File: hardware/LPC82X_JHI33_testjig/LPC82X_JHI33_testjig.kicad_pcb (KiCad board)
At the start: 2 copper layers, 23.6 x 23.5 mm, 80 parts, among them J1 LPC82XJHI33_LEFT, J2 LPC82XJHI33_RIGHT, J3 JTAG_2X05

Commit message: routing completed
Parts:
- removed C7: 2.2u, SquantorRcl:C_0805
- added H1: MountingHole, MountingHole:MountingHole_3.2mm_M3_Pad_Via, F.Cu at (73.7, 99.1)
- added H2: MountingHole, MountingHole:MountingHole_3.2mm_M3_Pad_Via, F.Cu at (73.7, 114.3)
- added H3: MountingHole, MountingHole:MountingHole_3.2mm_M3_Pad_Via, F.Cu at (104.1, 114.3)
- added H4: MountingHole, MountingHole:MountingHole_3.2mm_M3_Pad_Via, F.Cu at (104.1, 99.1)
- C1, C10, C11, C12, C13, C14, C15, C16, C17, C18, C19, C2, C20, C21, C22, C23, C24, C25, C3, C4, C5, C6, C8, C9: value 2.2u -> 1u; footprint SquantorRcl:C_0805 -> SquantorRcl:C_0402; moved to B.Cu
- J1: footprint SquantorConnectorsNamed:LPC82XJHI33_breakout_left -> SquantorConnectors:Header-0254-2X09-H015
- J2: footprint SquantorConnectorsNamed:LPC82XJHI33_breakout_right -> SquantorConnectors:Header-0254-2X09-H015
- R1, R11, R13, R15, R17, R19, R2, R21, R23, R25, R27, R29, R31, R33, R35, R37, R39, R41, R43, R45, R47, R49, R5, R51, R7, R9: footprint SquantorRcl:R_0603_hand -> SquantorRcl:R_0402_hand
- R10, R12, R14, R16, R18, R20, R22, R24, R26, R28, R30, R32, R34, R36, R38, R4, R40, R42, R44, R46, R48, R50, R6, R8: footprint SquantorRcl:R_0603_hand -> SquantorRcl:R_0402_hand; moved to B.Cu
- moved R12 82.3 mm to (94.0, 108.3)
- moved C5 80.8 mm to (91.7, 108.3), turned to 180 degrees
- moved R6 80.8 mm to (94.0, 101.8)
- moved C2 78.7 mm to (91.7, 101.8), turned to 180 degrees
- moved R22 70.9 mm to (94.0, 112.2)
- moved C11 69.7 mm to (91.7, 112.2), turned to 180 degrees
- moved R16 68.8 mm to (94.0, 110.9)
- moved R8 68.1 mm to (94.0, 105.7)
- moved R32 67.2 mm to (83.8, 104.4), turned to 180 degrees
- moved C8 67.2 mm to (91.7, 110.9), turned to 180 degrees
- moved R33 66.7 mm to (83.8, 104.4), turned to 180 degrees
- moved C3 66.0 mm to (91.7, 105.7), turned to 180 degrees
- moved R26 65.6 mm to (83.8, 100.5), turned to 180 degrees
- moved R27 65.6 mm to (83.8, 100.5), turned to 180 degrees
- moved C16 60.7 mm to (86.1, 104.4)
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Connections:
- J1 pad 10: /PIO0_26 -> /PIO0_27
- J1 pad 11: /PIO0_25 -> /PIO0_24
- J1 pad 12: /PIO0_24 -> /PIO0_25
- J1 pad 13: /PIO0_15 -> /PIO0_1
- J1 pad 14: /PIO0_1 -> /PIO0_15
- J1 pad 3: /PIO0_28 -> /PIO0_3
- J1 pad 4: /PIO0_3 -> /PIO0_28
- J1 pad 5: /PIO0_2 -> /PIO0_11
- J1 pad 6: /PIO0_11 -> /PIO0_2
- J1 pad 7: /PIO0_10 -> /PIO0_16
- J1 pad 8: /PIO0_16 -> /PIO0_10
- J1 pad 9: /PIO0_27 -> /PIO0_26
- J2 pad 10: /PIO0_21 -> /PIO0_20
- J2 pad 11: /PIO0_22 -> /PIO0_23
- J2 pad 12: /PIO0_23 -> /PIO0_22
- J2 pad 13: /PIO0_14 -> /PIO0_0
- J2 pad 14: /PIO0_0 -> /PIO0_14
- J2 pad 15: /PIO0_6 -> /PIO0_7
- J2 pad 16: /PIO0_7 -> /PIO0_6
- J2 pad 3: /PIO0_4 -> /PIO0_12
- J2 pad 4: /PIO0_12 -> /PIO0_4
- J2 pad 5: /PIO0_13 -> /PIO0_17
- J2 pad 6: /PIO0_17 -> /PIO0_13
- J2 pad 7: /PIO0_18 -> /PIO0_19
- J2 pad 8: /PIO0_19 -> /PIO0_18
- J2 pad 9: /PIO0_20 -> /PIO0_21
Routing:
- net /Digital_stimulus: track 0.00 -> 41.8 mm
- net /VDD: track 0.00 -> 41.6 mm
- net /VSS: track 12.7 -> 0.00 mm
- net /PIO0_15: track 0.00 -> 10.6 mm
- net /PIO0_7: track 0.00 -> 10.6 mm
- net /PIO0_25: track 0.00 -> 10.5 mm
- net /PIO0_0: track 0.00 -> 10.4 mm
- net /PIO0_17: track 0.00 -> 10.3 mm
- net /PIO0_10: track 0.00 -> 10.3 mm
- net /PIO0_27: track 0.00 -> 10.3 mm
- net /PIO0_23: track 0.00 -> 10.3 mm
- net /PIO0_19: track 0.00 -> 10.3 mm
- net /PIO0_28: track 0.00 -> 10.3 mm
- net /PIO0_21: track 0.00 -> 10.2 mm
- net /PIO0_12: track 0.00 -> 10.1 mm
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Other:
- board size 23.6 x 23.5 mm -> 38.8 x 23.5 mm

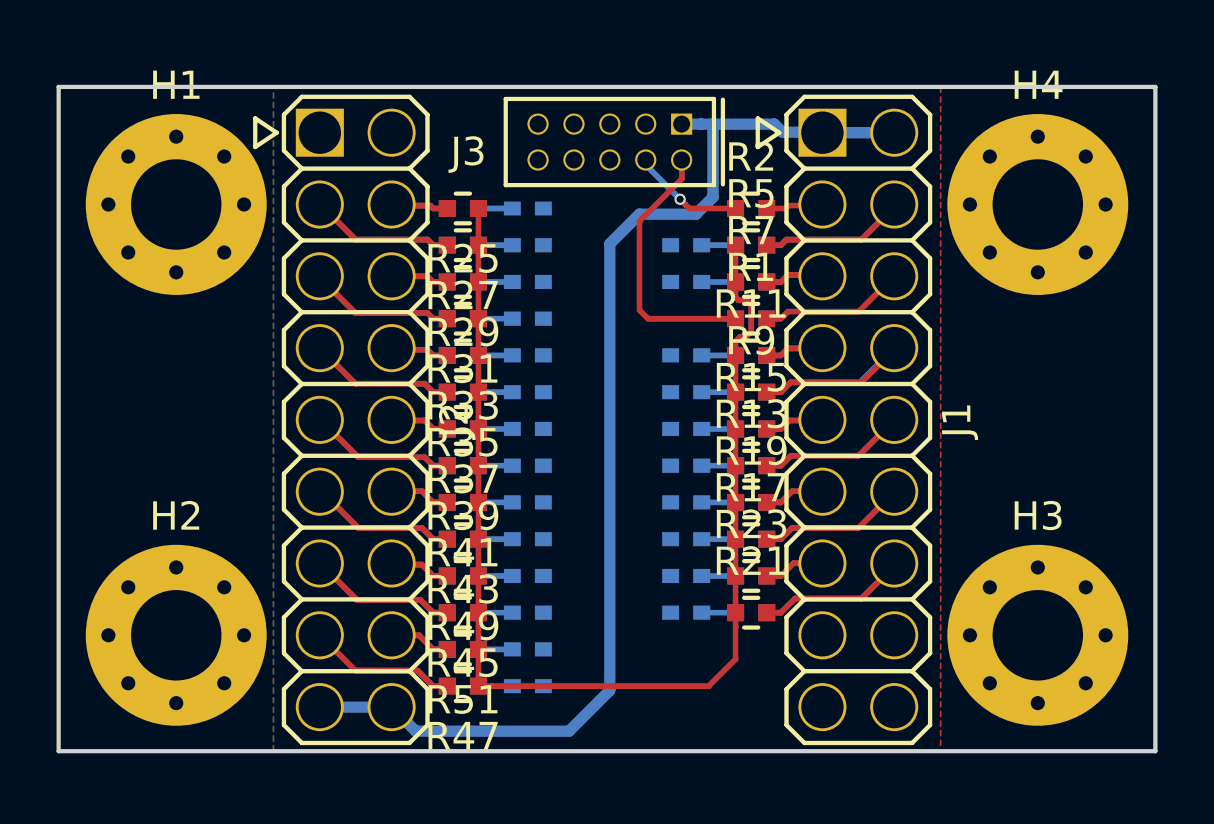
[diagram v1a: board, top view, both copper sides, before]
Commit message: silk placement completed (where possible)
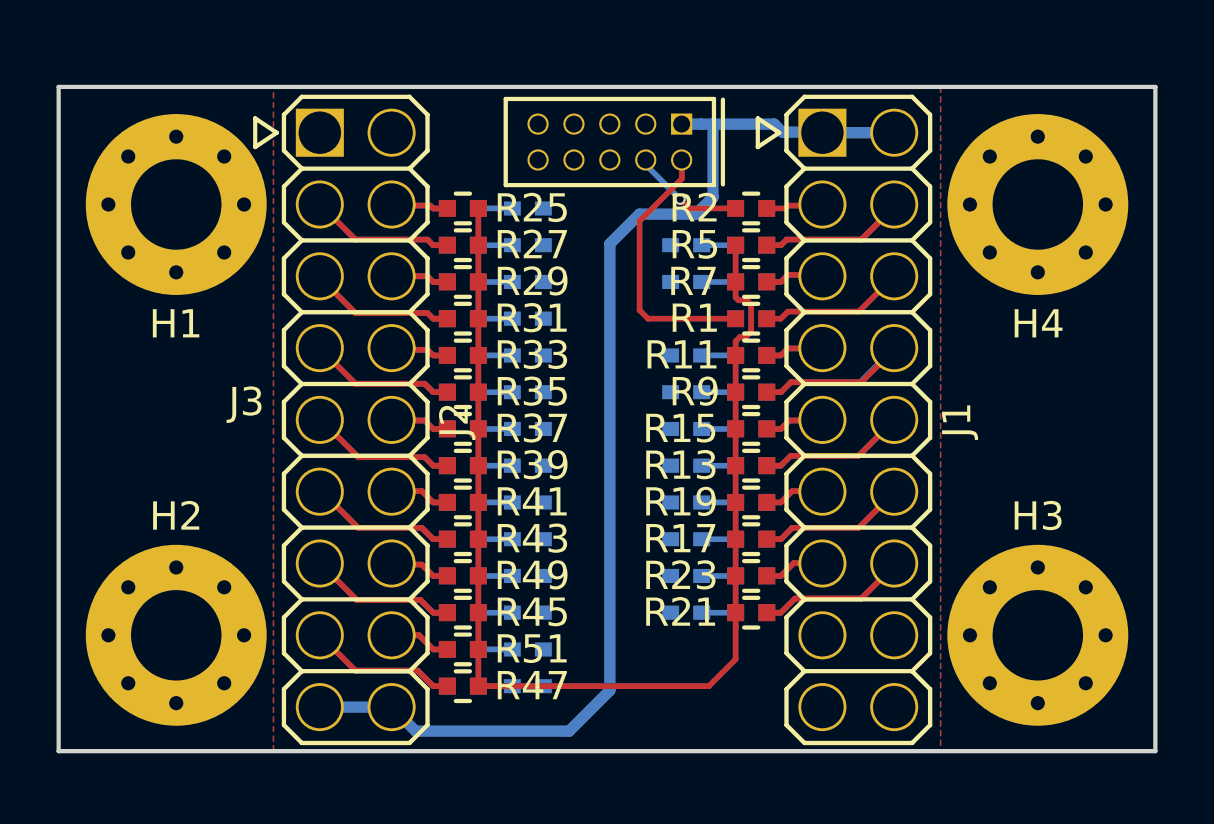
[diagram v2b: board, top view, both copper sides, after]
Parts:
- moved N1 15.3 mm to (73.4, 106.6)
- moved N2 0.90 mm to (88.5, 117.5)

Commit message: added RED led indicator
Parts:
- added D1: LED, SquantorDiodes:D_0603_hand, F.Cu at (94.2, 96.8)
- added R3: R_Small, SquantorRcl:R_0402_hand, B.Cu at (94.0, 96.8)
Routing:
- net Net-(D1-Pad2): track 0.00 -> 2.50 mm, vias 0 -> 1
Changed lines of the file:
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@@
     (thickness 1.6)
     (drawings 4)
-    (tracks 267)
+    (tracks 272)
     (zones 0)
-    (modules 83)
-    (nets 56)
+    (modules 85)
+    (nets 57)
   )
   (page A4)
@@
   )
   (setup
-    (last_trace_width 0.4)
+    (last_trace_width 0.2)
     (user_trace_width 0.127)
     (user_trace_width 0.2)
@@
   (net 54 "Net-(C25-Pad1)")
   (net 55 /Digital_stimulus)
+  (net 56 "Net-(D1-Pad2)")
   (net_class Default "This is the default net class."
     (clearance 0.127)
@@
     (add_net "Net-(C8-Pad1)")
     (add_net "Net-(C9-Pad1)")
+    (add_net "Net-(D1-Pad2)")
     (add_net "Net-(J1-Pad15)")
     (add_net "Net-(J1-Pad16)")
@@
     (add_net "Net-(J3-Pad8)")
   )
+  (module SquantorRcl:R_0402_hand (layer B.Cu)
+    (at 94 96.8 270)
+    (descr "Resistor SMD 0402, reflow soldering, Vishay (see dcrcw.pdf)")
+    (tags "resistor 0402")
+    (attr smd)
+    (fp_text reference R3 (at 0 1.8 270) (layer B.SilkS)
+      (effects (font (size 1 1) (thickness 0.15)) (justify mirror))
+    )
+    (fp_text value R_Small (at 0 -1.8 270) (layer B.Fab)
+      (effects (font (size 1 1) (thickness 0.15)) (justify mirror))
+    )
+    (fp_line (start -0.25 -0.525) (end 0.25 -0.525) (layer B.SilkS) (width 0.15))
+    (fp_line (start 0.25 0.525) (end -0.25 0.525) (layer B.SilkS) (width 0.15))
+    (fp_line (start 1.15 0.65) (end 1.15 -0.65) (layer B.CrtYd) (width 0.05))
+    (fp_line (start -1.15 0.65) (end -1.15 -0.65) (layer B.CrtYd) (width 0.05))
+    (fp_line (start -1.15 -0.65) (end 1.15 -0.65) (layer B.CrtYd) (width 0.05))
+    (fp_line (start -1.15 0.65) (end 1.15 0.65) (layer B.CrtYd) (width 0.05))
+    (fp_line (start -0.5 0.25) (end 0.5 0.25) (layer B.Fab) (width 0.1))
+    (fp_line (start 0.5 0.25) (end 0.5 -0.25) (layer B.Fab) (width 0.1))
+    (fp_line (start 0.5 -0.25) (end -0.5 -0.25) (layer B.Fab) (width 0.1))
+    (fp_line (start -0.5 -0.25) (end -0.5 0.25) (layer B.Fab) (width 0.1))
+    (pad 2 smd rect (at 0.55 0 270) (size 0.6 0.6) (layers B.Cu B.Paste B.Mask)
+      (net 56 "Net-(D1-Pad2)"))
+    (pad 1 smd rect (at -0.55 0 270) (size 0.6 0.6) (layers B.Cu B.Paste B.Mask)
+      (net 32 /VDD))
+    (model Resistors_SMD.3dshapes/R_0402.wrl
+      (at (xyz 0 0 0))
+      (scale (xyz 1 1 1))
+      (rotate (xyz 0 0 0))
+    )
+  )
+  (module SquantorDiodes:D_0603_hand (layer F.Cu)
+    (at 94.15 96.8 270)
+    (descr "Diode SMD 0603, reflow soldering, general purpose")
+    (tags "Diode 0603")
+    (attr smd)
+    (fp_text reference D1 (at 0 -1.9 90) (layer F.SilkS)
+      (effects (font (size 1 1) (thickness 0.15)))
+    )
+    (fp_text value LED (at 0 1.9 90) (layer F.Fab)
+      (effects (font (size 1 1) (thickness 0.15)))
+    )
+    (fp_line (start -0.3 -0.675) (end -0.3 0.675) (layer F.SilkS) (width 0.15))
+    (fp_line (start -0.3 -0.675) (end 0.5 -0.675) (layer F.SilkS) (width 0.15))
+    (fp_line (start 0.5 0.675) (end -0.3 0.675) (layer F.SilkS) (width 0.15))
+    (fp_line (start 1.5 -0.8) (end 1.5 0.8) (layer F.CrtYd) (width 0.05))
+    (fp_line (start -1.5 -0.8) (end -1.5 0.8) (layer F.CrtYd) (width 0.05))
+    (fp_line (start -1.5 0.8) (end 1.5 0.8) (layer F.CrtYd) (width 0.05))
+    (fp_line (start -1.5 -0.8) (end 1.5 -0.8) (layer F.CrtYd) (width 0.05))
+    (fp_line (start -0.8 -0.4) (end 0.8 -0.4) (layer F.Fab) (width 0.1))
+    (fp_line (start 0.8 -0.4) (end 0.8 0.4) (layer F.Fab) (width 0.1))
+    (fp_line (start 0.8 0.4) (end -0.8 0.4) (layer F.Fab) (width 0.1))
+    (fp_line (start -0.8 0.4) (end -0.8 -0.4) (layer F.Fab) (width 0.1))
+    (pad 2 smd rect (at 0.85 0 270) (size 0.7 0.9) (layers F.Cu F.Paste F.Mask)
+      (net 56 "Net-(D1-Pad2)"))
+    (pad 1 smd rect (at -0.85 0 270) (size 0.7 0.9) (layers F.Cu F.Paste F.Mask)
+      (net 31 /VSS))
+  )
   (module MountingHole:MountingHole_3.2mm_M3_Pad_Via (layer F.Cu)
     (at 104.14 99.06)
@@
   (segment (start 93.55 102.45) (end 93.45 102.35) (width 0.2) (layer F.Cu) (net 55))
   (segment (start 93.45 102.35) (end 93.45 100.5) (width 0.2) (layer F.Cu) (net 55))
+  (via (at 95.2 97.8) (size 0.4) (drill 0.254) (layers F.Cu B.Cu) (net 56))
+  (segment (start 94.15 97.65) (end 95.05 97.65) (width 0.2) (layer F.Cu) (net 56))
+  (segment (start 95.05 97.65) (end 95.2 97.8) (width 0.2) (layer F.Cu) (net 56))
+  (segment (start 95.2 97.8) (end 94.45 97.8) (width 0.2) (layer B.Cu) (net 56))
+  (segment (start 94.45 97.8) (end 94 97.35) (width 0.2) (layer B.Cu) (net 56))
   (zone (net 31) (net_name /VSS) (layer B.Cu) (hatch edge 0.508)
     (connect_pads (clearance 0.3))

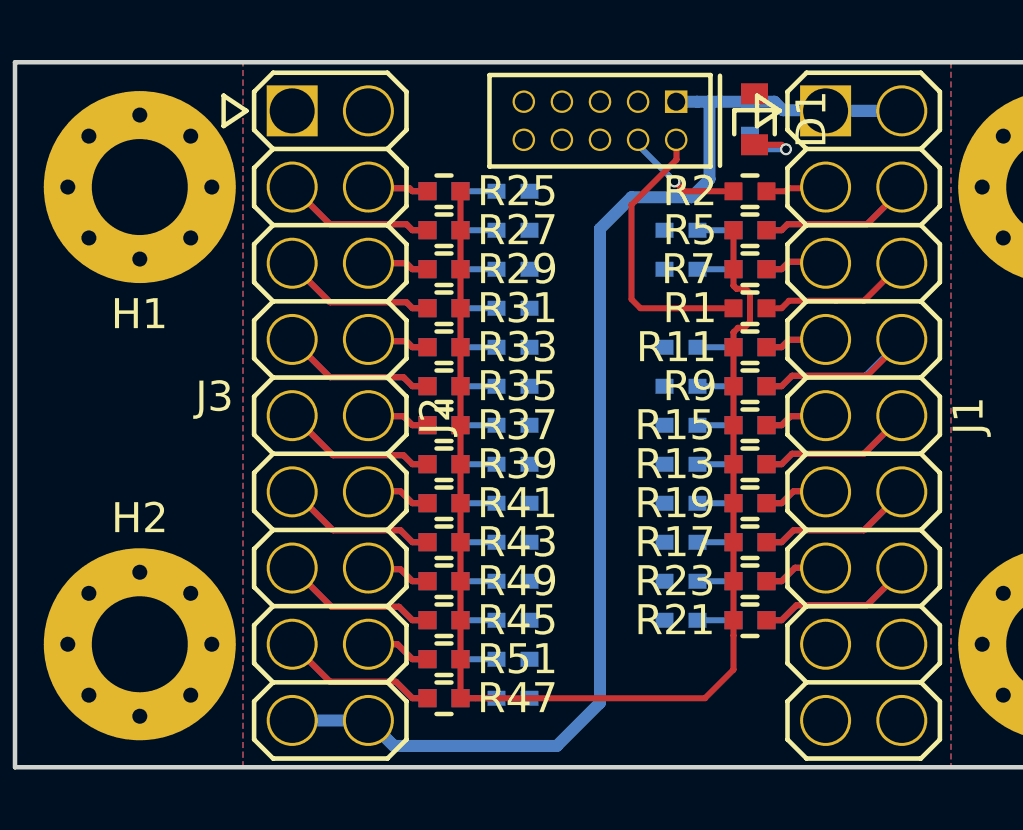
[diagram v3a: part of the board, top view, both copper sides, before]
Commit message: silk screen updates
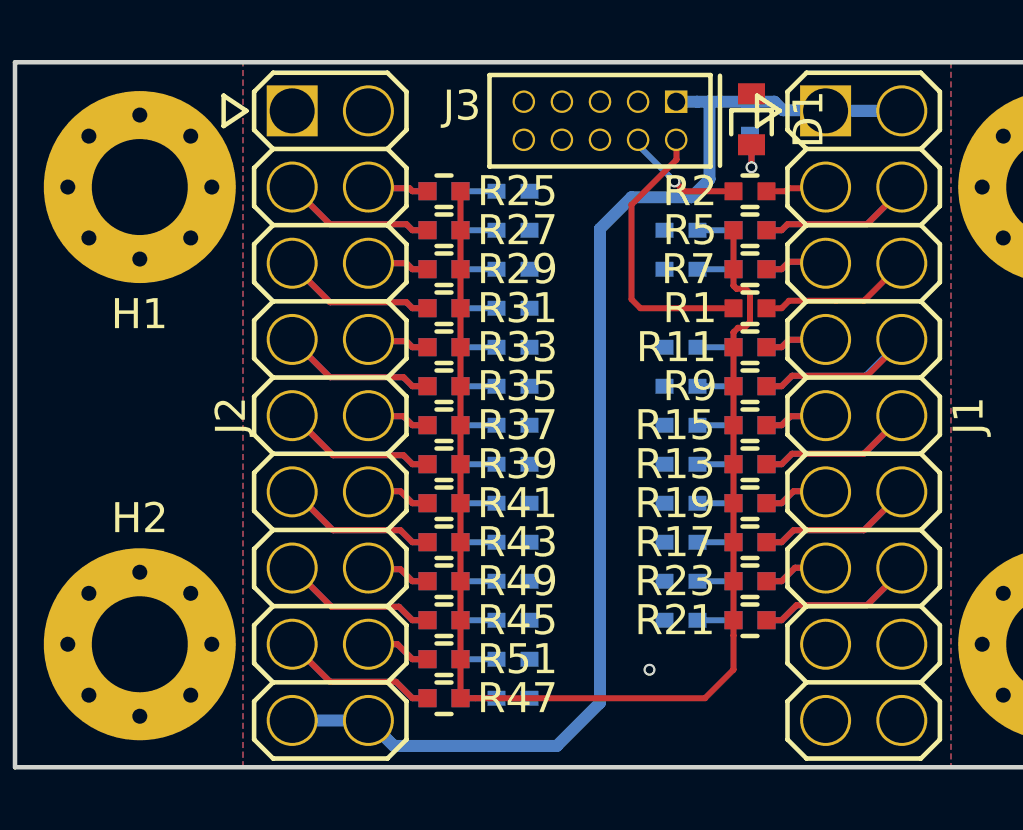
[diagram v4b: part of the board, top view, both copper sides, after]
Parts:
- moved D1 0.10 mm to (94.0, 96.8)
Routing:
- net Net-(D1-Pad2): track 2.50 -> 1.82 mm
- net /VSS: vias 0 -> 1
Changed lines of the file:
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@@
   )
   (module SquantorDiodes:D_0603_hand (layer F.Cu)
-    (at 94.15 96.8 270)
+    (at 94.05 96.8 270)
     (descr "Diode SMD 0603, reflow soldering, general purpose")
     (tags "Diode 0603")
@@
     (tags "pinheader 1.5mm 2.54mm")
     (attr virtual)
-    (fp_text reference J2 (at 0 -3.5 90) (layer F.SilkS)
+    (fp_text reference J2 (at 0 3.31 90) (layer F.SilkS)
       (effects (font (size 1 1) (thickness 0.15)))
     )
@@
   (module SquantorConnectors:Header-0127-2X05-H006 (layer F.Cu)
     (at 89 96.85 180)
-    (fp_text reference J3 (at 12.85 -9.2 180) (layer F.SilkS)
+    (fp_text reference J3 (at 4.6 0.5) (layer F.SilkS)
       (effects (font (size 1 1) (thickness 0.15)))
     )
@@
   (segment (start 93.45 99.2) (end 91.811937 99.2) (width 0.2) (layer F.Cu) (net 30))
   (via (at 91.484927 98.87299) (size 0.4) (drill 0.254) (layers F.Cu B.Cu) (net 30))
+  (via (at 90.65 115.15) (size 0.4) (drill 0.254) (layers F.Cu B.Cu) (net 31))
   (segment (start 96.52 96.52) (end 99.03 96.52) (width 0.4) (layer B.Cu) (net 32))
   (segment (start 99.03 96.52) (end 99.05 96.5) (width 0.4) (layer B.Cu) (net 32))
@@
   (segment (start 93.55 102.45) (end 93.45 102.35) (width 0.2) (layer F.Cu) (net 55))
   (segment (start 93.45 102.35) (end 93.45 100.5) (width 0.2) (layer F.Cu) (net 55))
-  (via (at 95.2 97.8) (size 0.4) (drill 0.254) (layers F.Cu B.Cu) (net 56))
-  (segment (start 94.15 97.65) (end 95.05 97.65) (width 0.2) (layer F.Cu) (net 56))
-  (segment (start 95.05 97.65) (end 95.2 97.8) (width 0.2) (layer F.Cu) (net 56))
-  (segment (start 95.2 97.8) (end 94.45 97.8) (width 0.2) (layer B.Cu) (net 56))
-  (segment (start 94.45 97.8) (end 94 97.35) (width 0.2) (layer B.Cu) (net 56))
+  (via (at 94.05 98.4) (size 0.4) (drill 0.254) (layers F.Cu B.Cu) (net 56))
+  (segment (start 94.05 97.65) (end 94.05 98.4) (width 0.2) (layer F.Cu) (net 56))
+  (segment (start 94.05 98.4) (end 94.05 97.4) (width 0.2) (layer B.Cu) (net 56))
+  (segment (start 94.05 97.4) (end 94 97.35) (width 0.2) (layer B.Cu) (net 56))
   (zone (net 31) (net_name /VSS) (layer B.Cu) (hatch edge 0.508)
     (connect_pads (clearance 0.3))
